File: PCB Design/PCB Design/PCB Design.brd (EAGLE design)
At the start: 120.6 x 88.6 mm, 6 parts, among them J1 1X2-3.5MM, U1 ADXL337

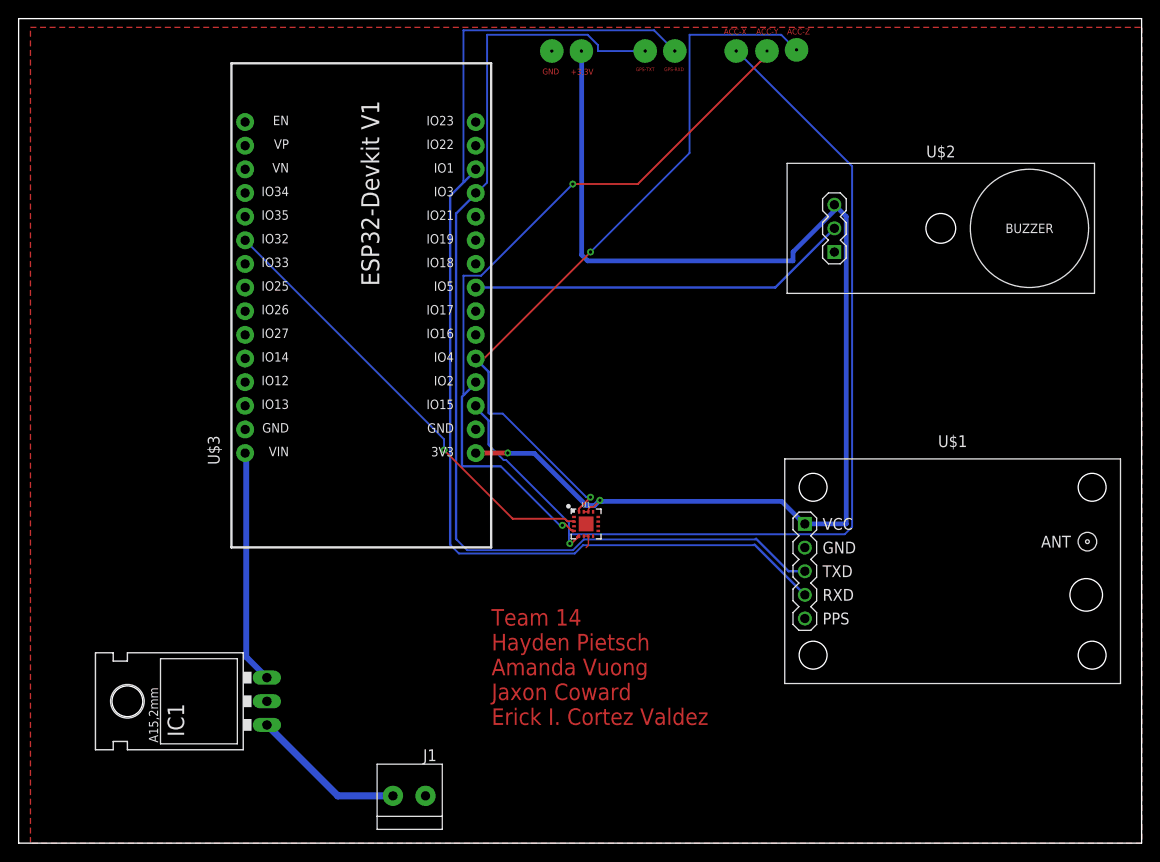
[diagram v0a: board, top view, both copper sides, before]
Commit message: Fixed Scematic and Board Based on Shawn's suggestions
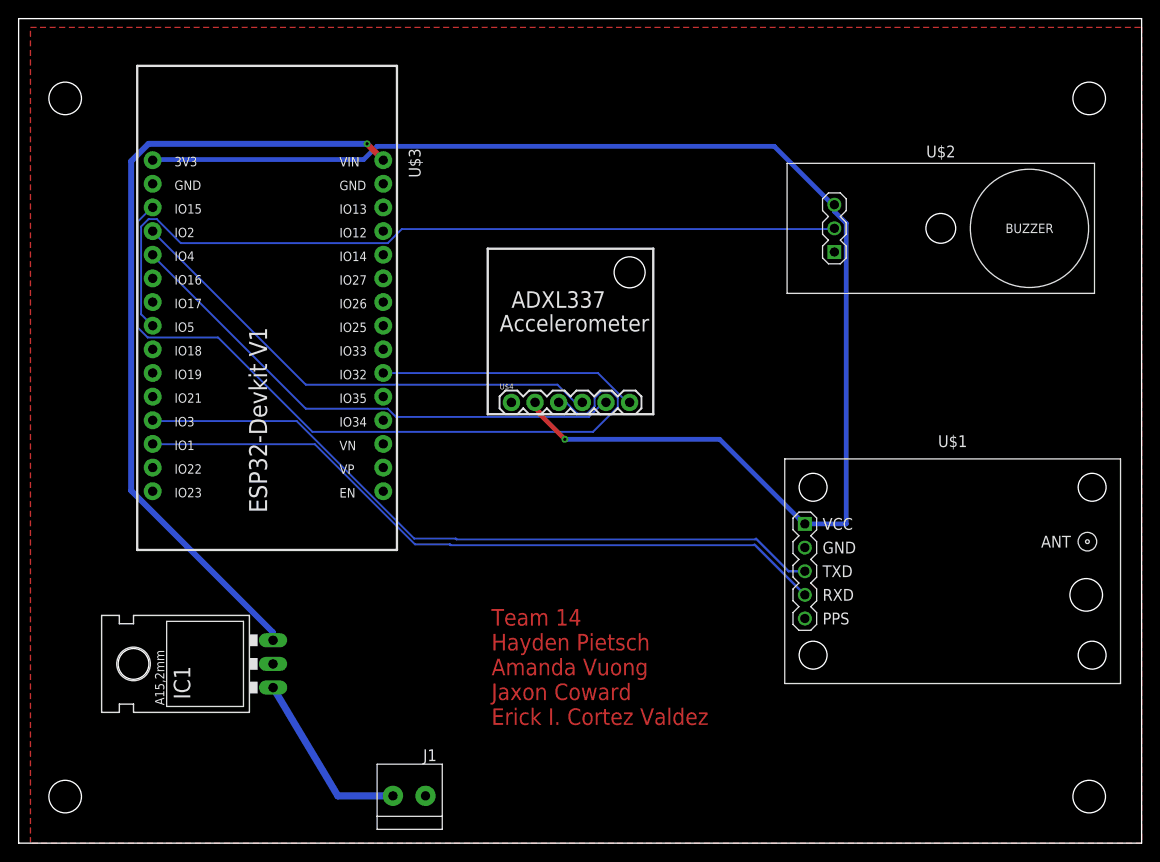
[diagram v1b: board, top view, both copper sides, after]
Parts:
- removed U1: ADXL337, SparkFun-Sensors:LFCSP-16-3X3
- added U$4: ADXL337_ACCELEROMETER, ADXL337_Breakout:ADXL337BREAKOUT
- moved U$3 16.2 mm to (27.9, 50.5), turned to 270 degrees
- moved IC1 4.07 mm to (23.5, 19.3)
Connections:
- net 3.3V: now also U$4.2; no longer U1.14, U1.15
- net GND: now also U$4.1; no longer U1.6, U1.7
- net N$3: now also U$4.6; no longer U1.2
- net N$6: now also U$4.3; no longer U1.5
- net N$7: now also U$4.4; no longer U1.4
- net N$8: now also U$4.5; no longer U1.16
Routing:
- net 5V: track 25.1 -> 86.4 mm, vias 0 -> 1
- net N$11: track 41.2 -> 87.7 mm
- net N$9: track 122.5 -> 76.8 mm, vias 1 -> 0
- net N$10: track 113.6 -> 76.9 mm, vias 1 -> 0
- net N$6: track 108.1 -> 80.6 mm, vias 2 -> 0
- net N$7: track 80.9 -> 53.8 mm, vias 3 -> 0
- net N$8: track 80.2 -> 56.6 mm, vias 3 -> 0
- net N$3: track 48.5 -> 27.8 mm, vias 1 -> 0
- net 3.3V: track 134.2 -> 151.2 mm, vias 3 -> 1
- net VIN: track 16.7 -> 19.5 mm
- net GND: track 1.84 -> 0.00 mm, vias 1 -> 0
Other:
- board text removed: "+3.3V"
- board text removed: "ACC-X"
- board text removed: "ACC-Y"
- board text removed: "ACC-Z"
- board text removed: "GND"
- board text removed: "GPS-RXD"
- board text removed: "GPS-TXT"
